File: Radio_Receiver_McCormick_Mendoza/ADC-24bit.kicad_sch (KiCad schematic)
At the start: 39 parts, among them J21 SDR Out, J41 V_DIV, J42 VDDA/2, U10 OPA1612AID, U12 PCM1808PWR

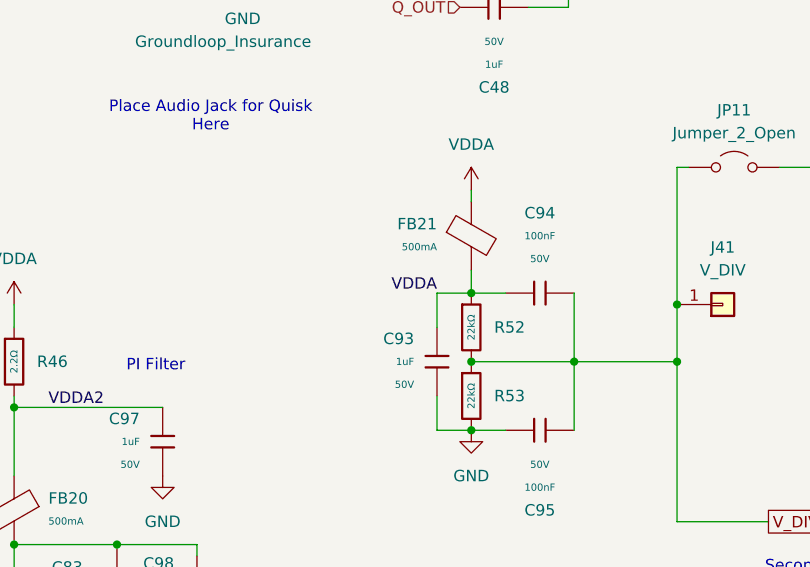
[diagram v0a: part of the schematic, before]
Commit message: Finished routing master copy and added GND and PWR planes with vias
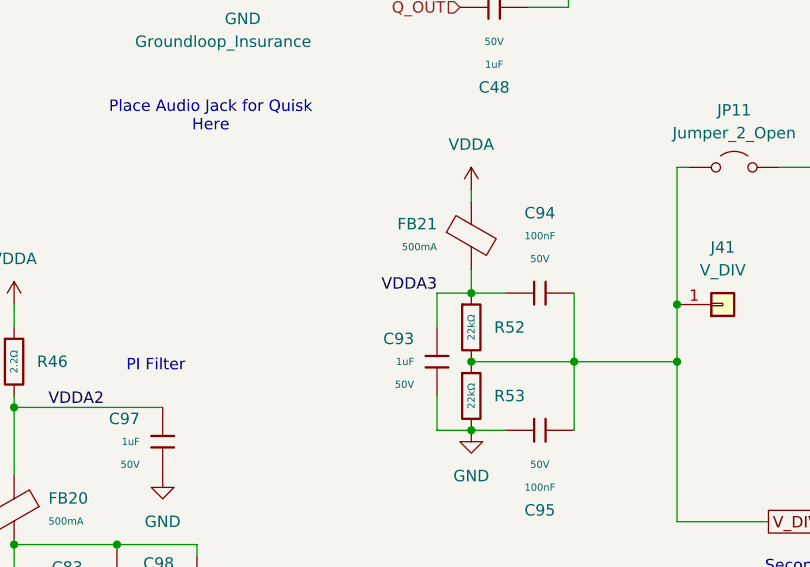
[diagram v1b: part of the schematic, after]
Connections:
- net VDDA: no longer C93.1, C94.2, FB21.2, R52.1
- new net VDDA3: C93.1, C94.2, FB21.2, R52.1
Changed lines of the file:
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@@
 		)
 	)
-	(label "VDDA"
+	(label "VDDA3"
 		(at 73.66 121.92 180)
 		(effects
